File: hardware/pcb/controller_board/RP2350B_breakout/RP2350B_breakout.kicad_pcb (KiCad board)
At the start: 2 copper layers, 54 parts, among them J1 USB_B_Micro, J2 430450828, J4 SM03B-SRSS-TB, J6 debug, SW1 SW_Push, SW2 SW_Push, U1 RP2350_80QFN, U2 NCP1117-3.3_SOT223, U3 W25Q128JVS, U5 ISO7730FDWR, U6 AM26LS31CD, Y1 ABM8-272-T3

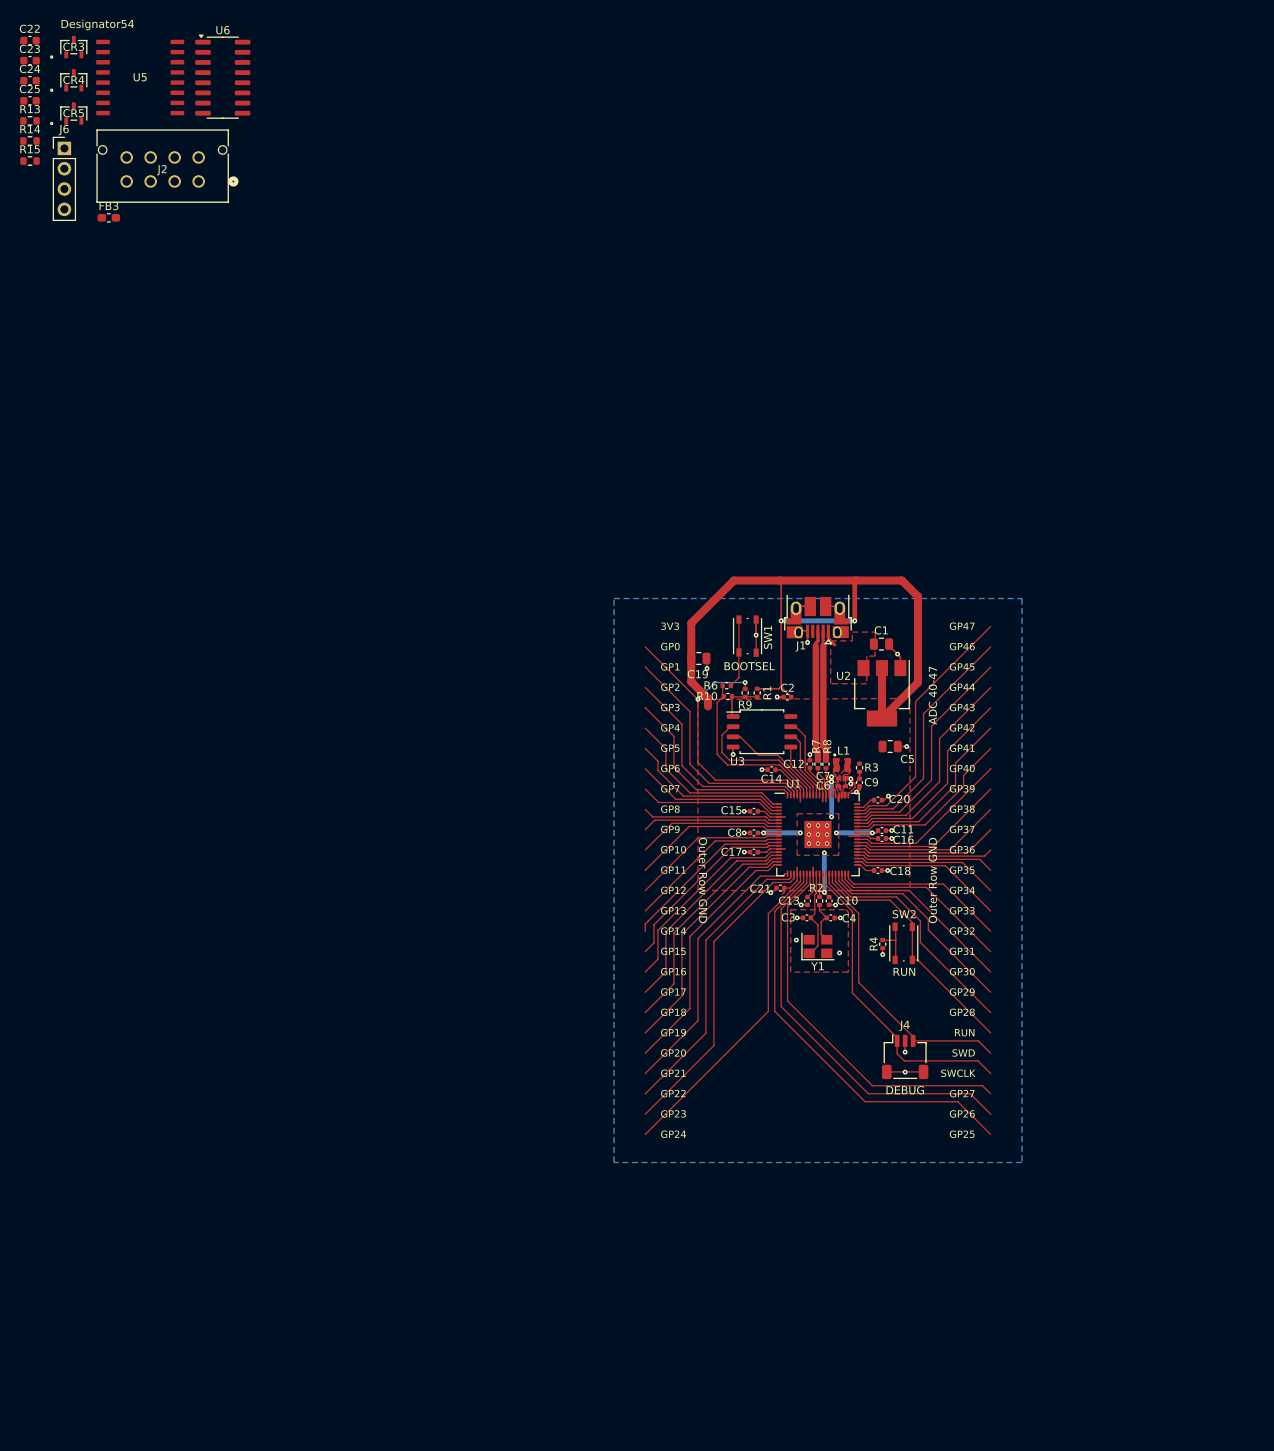
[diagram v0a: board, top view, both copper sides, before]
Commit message: KiCAD files for 6 axis RP2350B board
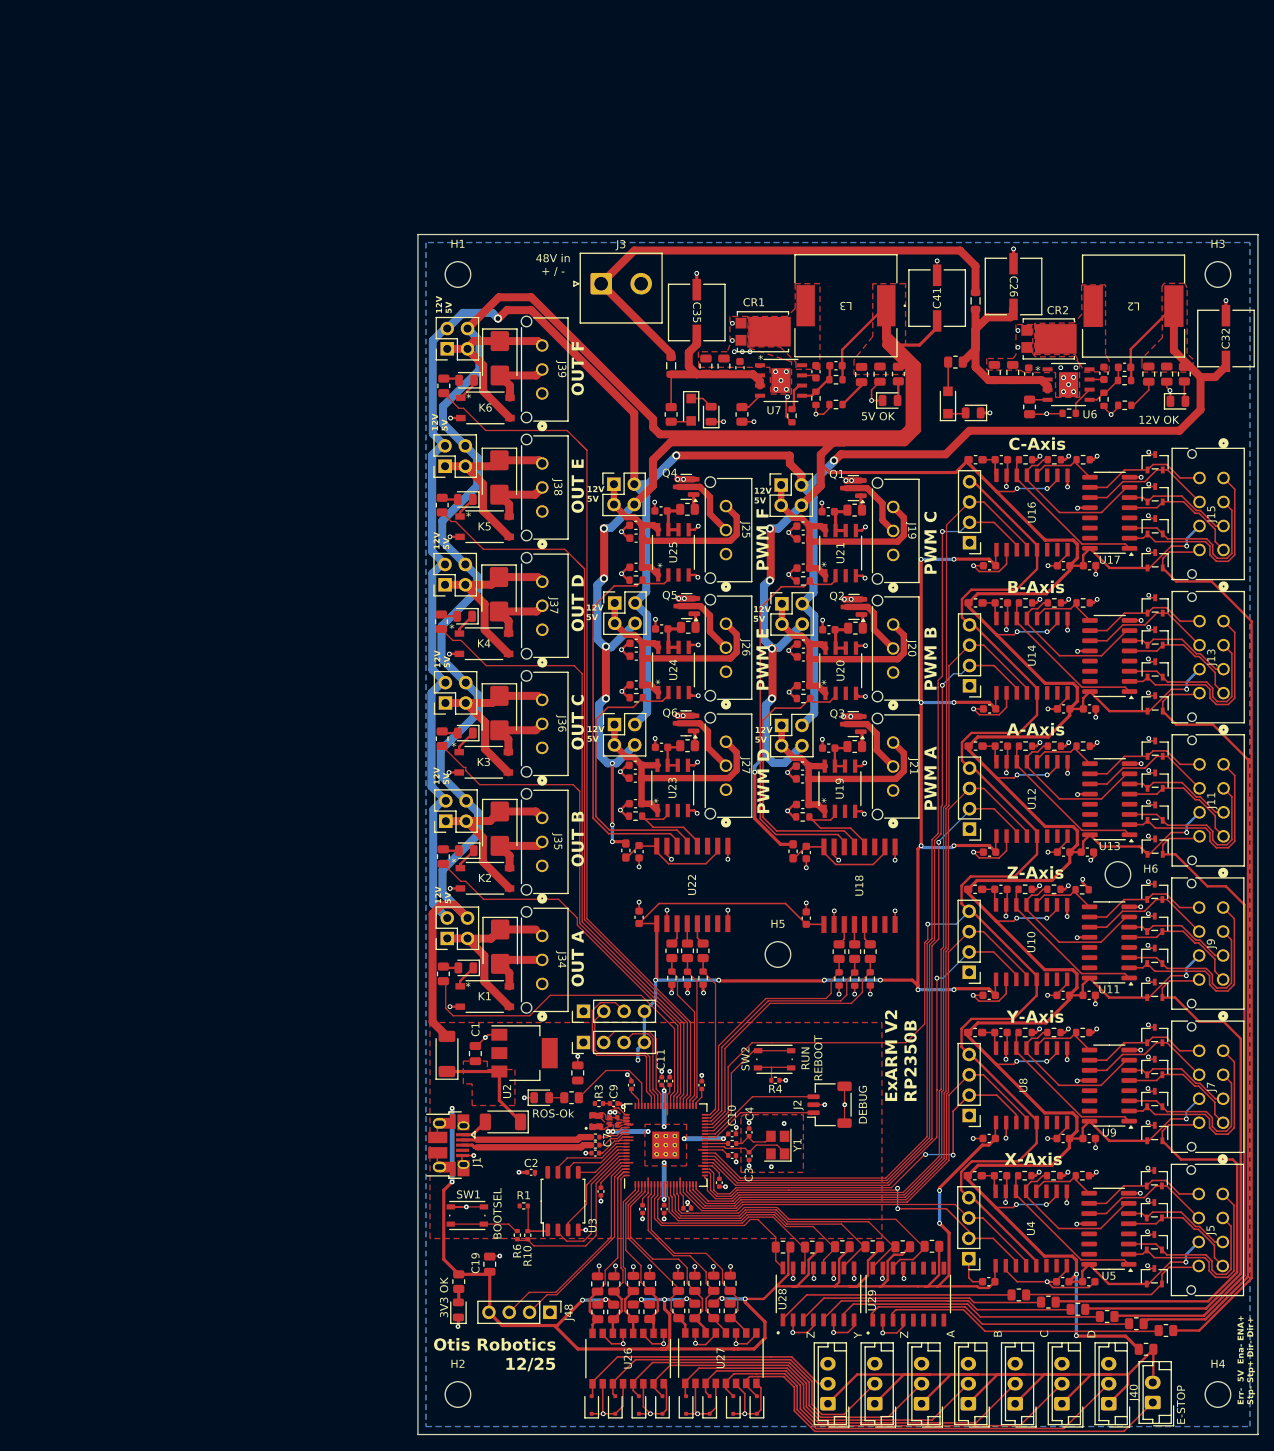
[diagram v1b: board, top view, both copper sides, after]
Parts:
- removed the J2 at (22.6, 18.4)
- added C26: EEE-FK1H470XP, CAP_EEFK_D8_PAN:CAP_EEFK_D8_PAN-L, F.Cu at (124.5, 31.5)
- added C27: 2.2uF, Capacitor_SMD:C_0805_2012Metric, F.Cu at (122.0, 42.2)
- added C28: 2.2uF, Capacitor_SMD:C_0805_2012Metric, F.Cu at (124.3, 42.2)
- added C29: 0.1uF, Capacitor_SMD:C_0603_1608Metric, F.Cu at (126.3, 42.5)
- added C30: 2.2nF, Capacitor_SMD:C_0603_1608Metric, F.Cu at (135.8, 42.4)
- added C31: 50pF, Capacitor_SMD:C_0603_1608Metric, F.Cu at (138.3, 41.6)
- added C32: EEE-FK1H470XP, CAP_EEFK_D8_PAN:CAP_EEFK_D8_PAN-L, F.Cu at (151.0, 38.0)
- added C33: 22uF, Capacitor_SMD:C_0805_2012Metric, F.Cu at (141.3, 42.5)
- added C34: 22uF, Capacitor_SMD:C_0805_2012Metric, F.Cu at (143.6, 42.5)
- added C35: EEE-FK1H470XP, CAP_EEFK_D8_PAN:CAP_EEFK_D8_PAN-L, F.Cu at (84.8, 34.8)
- added C36: 2.2uF, Capacitor_SMD:C_0805_2012Metric, F.Cu at (88.2, 41.5)
- added C37: 2.2uF, Capacitor_SMD:C_0805_2012Metric, F.Cu at (86.0, 41.5)
- added C38: 0.1uF, Capacitor_SMD:C_0603_1608Metric, F.Cu at (90.2, 41.6)
- added C39: 2.2nF, Capacitor_SMD:C_0603_1608Metric, F.Cu at (99.8, 42.1)
- added C40: 65pF, Capacitor_SMD:C_0603_1608Metric, F.Cu at (102.2, 41.4)
- added C41: EEE-FK1H470XP, CAP_EEFK_D8_PAN:CAP_EEFK_D8_PAN-L, F.Cu at (114.9, 32.9)
- added C42: 22uF, Capacitor_SMD:C_0805_2012Metric, F.Cu at (105.5, 42.5)
- added C43: 22uF, Capacitor_SMD:C_0805_2012Metric, F.Cu at (107.8, 42.5)
- added C44: 100nF, Capacitor_SMD:C_0603_1608Metric, F.Cu at (121.4, 138.0)
- added C45: 100nF, Capacitor_SMD:C_0603_1608Metric, F.Cu at (122.9, 124.8)
- added C46: 1uF, Capacitor_SMD:C_0603_1608Metric, F.Cu at (133.9, 138.0)
- added C47: 100nF, Capacitor_SMD:C_0603_1608Metric, F.Cu at (130.7, 138.0)
- added C48: 100nF, Capacitor_SMD:C_0603_1608Metric, F.Cu at (121.4, 120.1)
- added C49: 100nF, Capacitor_SMD:C_0603_1608Metric, F.Cu at (122.9, 106.8)
- added C50: 1uF, Capacitor_SMD:C_0603_1608Metric, F.Cu at (133.9, 120.1)
- added C51: 100nF, Capacitor_SMD:C_0603_1608Metric, F.Cu at (130.7, 120.1)
- added C52: 100nF, Capacitor_SMD:C_0603_1608Metric, F.Cu at (121.5, 102.2)
- added C53: 100nF, Capacitor_SMD:C_0603_1608Metric, F.Cu at (122.9, 89.0)
- added C54: 1uF, Capacitor_SMD:C_0603_1608Metric, F.Cu at (133.7, 102.2)
- added C55: 100nF, Capacitor_SMD:C_0603_1608Metric, F.Cu at (130.7, 102.2)
- added C56: 100nF, Capacitor_SMD:C_0603_1608Metric, F.Cu at (121.5, 84.3)
- added C57: 100nF, Capacitor_SMD:C_0603_1608Metric, F.Cu at (122.9, 71.0)
- added C58: 1uF, Capacitor_SMD:C_0603_1608Metric, F.Cu at (133.9, 84.3)
- added C59: 100nF, Capacitor_SMD:C_0603_1608Metric, F.Cu at (130.7, 84.3)
- added C60: 100nF, Capacitor_SMD:C_0603_1608Metric, F.Cu at (121.5, 66.4)
- added C61: 100nF, Capacitor_SMD:C_0603_1608Metric, F.Cu at (122.9, 53.1)
- added C62: 1uF, Capacitor_SMD:C_0603_1608Metric, F.Cu at (133.9, 66.4)
- added C63: 100nF, Capacitor_SMD:C_0603_1608Metric, F.Cu at (130.7, 66.4)
- added C64: 100nF, Capacitor_SMD:C_0603_1608Metric, F.Cu at (98.5, 110.5)
- added C65: 100nF, Capacitor_SMD:C_0603_1608Metric, F.Cu at (98.5, 102.3)
- added C66: 100nF, Capacitor_SMD:C_0603_1608Metric, F.Cu at (98.1, 96.3)
- added C67: 100nF, Capacitor_SMD:C_0603_1608Metric, F.Cu at (98.2, 81.4)
- added C68: 100nF, Capacitor_SMD:C_0603_1608Metric, F.Cu at (98.2, 66.7)
- added C69: 100nF, Capacitor_SMD:C_0603_1608Metric, F.Cu at (98.1, 91.5)
- added C70: 100nF, Capacitor_SMD:C_0603_1608Metric, F.Cu at (98.2, 76.2)
- added C71: 25pF, Capacitor_SMD:C_0603_1608Metric, F.Cu at (101.3, 89.2)
- added C72: 100nF, Capacitor_SMD:C_0603_1608Metric, F.Cu at (98.1, 61.5)
- added C73: 25pF, Capacitor_SMD:C_0603_1608Metric, F.Cu at (101.4, 74.4)
- added C74: 25pF, Capacitor_SMD:C_0603_1608Metric, F.Cu at (101.3, 59.7)
- added C75: 1uF, Capacitor_SMD:C_0603_1608Metric, F.Cu at (98.1, 93.1)
- added C76: 1uF, Capacitor_SMD:C_0603_1608Metric, F.Cu at (98.2, 77.8)
- added C77: 1uF, Capacitor_SMD:C_0603_1608Metric, F.Cu at (98.2, 63.1)
- added C78: 100nF, Capacitor_SMD:C_0603_1608Metric, F.Cu at (77.6, 110.4)
- added C79: 100nF, Capacitor_SMD:C_0603_1608Metric, F.Cu at (77.6, 102.2)
- added C80: 100nF, Capacitor_SMD:C_0603_1608Metric, F.Cu at (77.2, 96.2)
- added C81: 100nF, Capacitor_SMD:C_0603_1608Metric, F.Cu at (77.3, 81.3)
- added C82: 100nF, Capacitor_SMD:C_0603_1608Metric, F.Cu at (77.3, 66.6)
- added C83: 100nF, Capacitor_SMD:C_0603_1608Metric, F.Cu at (77.2, 91.4)
- added C84: 100nF, Capacitor_SMD:C_0603_1608Metric, F.Cu at (77.3, 76.1)
- added C85: 25pF, Capacitor_SMD:C_0603_1608Metric, F.Cu at (80.5, 89.1)
- added C86: 100nF, Capacitor_SMD:C_0603_1608Metric, F.Cu at (77.2, 61.4)
- added C87: 25pF, Capacitor_SMD:C_0603_1608Metric, F.Cu at (80.5, 74.3)
- added C88: 25pF, Capacitor_SMD:C_0603_1608Metric, F.Cu at (80.4, 59.6)
- added C89: 1uF, Capacitor_SMD:C_0603_1608Metric, F.Cu at (77.2, 93.0)
- added C90: 1uF, Capacitor_SMD:C_0603_1608Metric, F.Cu at (77.3, 77.7)
- added C91: 1uF, Capacitor_SMD:C_0603_1608Metric, F.Cu at (77.3, 63.0)
- added C92: 100nF, Capacitor_SMD:C_0805_2012Metric, F.Cu at (74.5, 156.2)
- added C93: 100nF, Capacitor_SMD:C_0805_2012Metric, F.Cu at (76.9, 156.1)
- added C94: 100nF, Capacitor_SMD:C_0805_2012Metric, F.Cu at (79.0, 156.1)
- added C95: 100nF, Capacitor_SMD:C_0805_2012Metric, F.Cu at (82.6, 156.1)
- added C96: 100nF, Capacitor_SMD:C_0805_2012Metric, F.Cu at (84.6, 156.1)
- added C97: 100nF, Capacitor_SMD:C_0805_2012Metric, F.Cu at (89.0, 156.1)
- added C98: 100nF, Capacitor_SMD:C_0805_2012Metric, F.Cu at (72.5, 156.2)
- added C99: 100nF, Capacitor_SMD:C_0805_2012Metric, F.Cu at (87.0, 156.1)
- added CR1: SS5P10-M3/86A, SS5P10-M3-86A:DIODE_TO-277A-L, F.Cu at (93.1, 37.1)
- added CR10: PESD2CAN_215, PESD2CAN_215:SOT23_TO-236AB_NEX-L, F.Cu at (142.1, 137.3)
- added CR11: PESD2CAN_215, PESD2CAN_215:SOT23_TO-236AB_NEX-L, F.Cu at (142.1, 115.2)
- added CR12: PESD2CAN_215, PESD2CAN_215:SOT23_TO-236AB_NEX-L, F.Cu at (142.1, 111.2)
- added CR13: PESD2CAN_215, PESD2CAN_215:SOT23_TO-236AB_NEX-L, F.Cu at (142.1, 107.2)
- added CR14: PESD2CAN_215, PESD2CAN_215:SOT23_TO-236AB_NEX-L, F.Cu at (142.1, 119.4)
- added CR15: PESD2CAN_215, PESD2CAN_215:SOT23_TO-236AB_NEX-L, F.Cu at (142.2, 97.3)
- added CR16: PESD2CAN_215, PESD2CAN_215:SOT23_TO-236AB_NEX-L, F.Cu at (142.2, 93.3)
- added CR17: PESD2CAN_215, PESD2CAN_215:SOT23_TO-236AB_NEX-L, F.Cu at (142.2, 89.3)
- added CR18: PESD2CAN_215, PESD2CAN_215:SOT23_TO-236AB_NEX-L, F.Cu at (142.2, 101.5)
- added CR19: PESD2CAN_215, PESD2CAN_215:SOT23_TO-236AB_NEX-L, F.Cu at (142.2, 79.4)
- added CR2: SS5P10-M3/86A, SS5P10-M3-86A:DIODE_TO-277A-L, F.Cu at (128.9, 38.0)
- added CR20: PESD2CAN_215, PESD2CAN_215:SOT23_TO-236AB_NEX-L, F.Cu at (142.2, 75.4)
- added CR21: PESD2CAN_215, PESD2CAN_215:SOT23_TO-236AB_NEX-L, F.Cu at (142.2, 71.4)
- added CR22: PESD2CAN_215, PESD2CAN_215:SOT23_TO-236AB_NEX-L, F.Cu at (142.2, 83.6)
- added CR23: PESD2CAN_215, PESD2CAN_215:SOT23_TO-236AB_NEX-L, F.Cu at (142.2, 61.5)
- added CR24: PESD2CAN_215, PESD2CAN_215:SOT23_TO-236AB_NEX-L, F.Cu at (142.2, 57.5)
- added CR25: PESD2CAN_215, PESD2CAN_215:SOT23_TO-236AB_NEX-L, F.Cu at (142.2, 53.5)
- added CR26: PESD2CAN_215, PESD2CAN_215:SOT23_TO-236AB_NEX-L, F.Cu at (142.2, 65.7)
- added CR6: PESD2CAN_215, PESD2CAN_215:SOT23_TO-236AB_NEX-L, F.Cu at (142.1, 155.2)
- added CR7: PESD2CAN_215, PESD2CAN_215:SOT23_TO-236AB_NEX-L, F.Cu at (142.1, 133.1)
- added CR8: PESD2CAN_215, PESD2CAN_215:SOT23_TO-236AB_NEX-L, F.Cu at (142.1, 129.1)
- added CR9: PESD2CAN_215, PESD2CAN_215:SOT23_TO-236AB_NEX-L, F.Cu at (142.1, 125.1)
- added D1: D_Zener, Diode_SMD:Nexperia_CFP3_SOD-123W, F.Cu at (84.2, 46.9)
- added D10: LED (red), LED_SMD:LED_0805_2012Metric, F.Cu at (56.0, 102.0)
- added D11: LED (red), LED_SMD:LED_0805_2012Metric, F.Cu at (55.9, 87.3)
- added D12: LED (red), LED_SMD:LED_0805_2012Metric, F.Cu at (55.8, 72.7)
- added D13: LED (red), LED_SMD:LED_0805_2012Metric, F.Cu at (55.9, 58.1)
- added D14: LED (red), LED_SMD:LED_0805_2012Metric, F.Cu at (56.1, 43.2)
- added D15: SM6T39AY, Diode_SMD:D_SMB, F.Cu at (60.3, 114.0)
- added D16: SM6T39AY, Diode_SMD:D_SMB, F.Cu at (60.2, 99.3)
- added D17: SM6T39AY, Diode_SMD:D_SMB, F.Cu at (60.2, 84.8)
- added D18: SM6T39AY, Diode_SMD:D_SMB, F.Cu at (60.1, 70.0)
- added D19: SM6T39AY, Diode_SMD:D_SMB, F.Cu at (60.2, 55.4)
- added D2: LED, LED_SMD:LED_0805_2012Metric, F.Cu at (86.7, 47.5)
- added D20: SM6T39AY, Diode_SMD:D_SMB, F.Cu at (60.2, 40.5)
- added D21: BAT54J, Diode_SMD:D_SOD-323F, F.Cu at (71.7, 171.3)
- added D22: BAT54J, Diode_SMD:D_SOD-323F, F.Cu at (74.7, 171.3)
- added D23: BAT54J, Diode_SMD:D_SOD-323F, F.Cu at (77.6, 171.3)
- added D24: BAT54J, Diode_SMD:D_SOD-323F, F.Cu at (80.6, 171.3)
- added D25: BAT54J, Diode_SMD:D_SOD-323F, F.Cu at (83.5, 171.3)
- added D26: BAT54J, Diode_SMD:D_SOD-323F, F.Cu at (86.5, 171.3)
- added D27: BAT54J, Diode_SMD:D_SOD-323F, F.Cu at (89.4, 171.3)
- added D28: BAT54J, Diode_SMD:D_SOD-323F, F.Cu at (92.4, 171.3)
- added D29: LED, LED_SMD:LED_0805_2012Metric, F.Cu at (55.1, 159.4)
- added D3: LED, LED_SMD:LED_0805_2012Metric, F.Cu at (109.0, 45.8)
- added D30: LED, LED_SMD:LED_0805_2012Metric, F.Cu at (65.5, 132.9)
- added D4: D_Zener, Diode_SMD:Nexperia_CFP3_SOD-123W, F.Cu at (116.2, 46.0)
- added D5: LED, LED_SMD:LED_0805_2012Metric, F.Cu at (119.4, 47.3)
- added D6: LED, LED_SMD:LED_0805_2012Metric, F.Cu at (145.0, 45.9)
- added D7: LED (red), LED_SMD:LED_0805_2012Metric, F.Cu at (56.0, 116.7)
- added D8: PMEG4010EP,115, Diode_SMD:D_SOD-128, F.Cu at (60.6, 135.9)
- added D9: PMEG4010EP,115, Diode_SMD:D_SOD-128, F.Cu at (53.6, 127.4)
- added FB1: FerriteBead, Inductor_SMD:L_0805_2012Metric, F.Cu at (81.7, 41.4)
- added FB10: FerriteBead, Inductor_SMD:L_0603_1608Metric_Pad1.05x0.95mm_HandSolder, F.Cu at (76.0, 102.0)
- added FB2: FerriteBead, Inductor_SMD:L_0805_2012Metric, F.Cu at (119.7, 33.3)
- added FB4: FerriteBead, Inductor_SMD:L_0603_1608Metric_Pad1.05x0.95mm_HandSolder, F.Cu at (119.7, 124.8)
- added FB5: FerriteBead, Inductor_SMD:L_0603_1608Metric_Pad1.05x0.95mm_HandSolder, F.Cu at (119.7, 106.8)
- added FB6: FerriteBead, Inductor_SMD:L_0603_1608Metric_Pad1.05x0.95mm_HandSolder, F.Cu at (119.7, 89.0)
- added FB7: FerriteBead, Inductor_SMD:L_0603_1608Metric_Pad1.05x0.95mm_HandSolder, F.Cu at (119.7, 71.0)
- added FB8: FerriteBead, Inductor_SMD:L_0603_1608Metric_Pad1.05x0.95mm_HandSolder, F.Cu at (119.7, 53.1)
- added FB9: FerriteBead, Inductor_SMD:L_0603_1608Metric_Pad1.05x0.95mm_HandSolder, F.Cu at (96.9, 102.1)
- added H1: MountingHole, MountingHole:MountingHole_3.2mm_M3_ISO7380, F.Cu at (55.0, 30.0)
- added H2: MountingHole, MountingHole:MountingHole_3.2mm_M3_ISO7380, F.Cu at (55.0, 170.0)
- added H3: MountingHole, MountingHole:MountingHole_3.2mm_M3_ISO7380, F.Cu at (150.0, 30.0)
- added H4: MountingHole, MountingHole:MountingHole_3.2mm_M3_ISO7380, F.Cu at (150.0, 170.0)
- added H5: MountingHole, MountingHole:MountingHole_3.2mm_M3_ISO7380, F.Cu at (95.0, 115.0)
- added H6: MountingHole, MountingHole:MountingHole_3.2mm_M3_ISO7380, F.Cu at (137.5, 105.0)
- added J10: debug, Connector_PinHeader_2.54mm:PinHeader_1x04_P2.54mm_Vertical, F.Cu at (119.0, 99.3)
- added J11: 430450828, 430450828:CONN_SD-43045-010_08_MOL, F.Cu at (150.7, 91.2)
- added J12: debug, Connector_PinHeader_2.54mm:PinHeader_1x04_P2.54mm_Vertical, F.Cu at (119.0, 81.4)
- added J13: 430450828, 430450828:CONN_SD-43045-010_08_MOL, F.Cu at (150.7, 73.3)
- added J14: debug, Connector_PinHeader_2.54mm:PinHeader_1x04_P2.54mm_Vertical, F.Cu at (119.0, 63.5)
- added J15: 430450828, 430450828:CONN_SD-43045-010_08_MOL, F.Cu at (150.7, 55.4)
- added J16: Conn_02x02_Odd_Even, Connector_PinHeader_2.54mm:PinHeader_2x02_P2.54mm_Vertical, F.Cu at (95.5, 86.4)
- added J17: Conn_02x02_Odd_Even, Connector_PinHeader_2.54mm:PinHeader_2x02_P2.54mm_Vertical, F.Cu at (95.5, 71.2)
- added J18: Conn_02x02_Odd_Even, Connector_PinHeader_2.54mm:PinHeader_2x02_P2.54mm_Vertical, F.Cu at (95.4, 56.3)
- added J19: 436500328, 436500328:CONN_SD-43650-010_03_MOL, F.Cu at (109.7, 62.1)
- added J20: 436500328, 436500328:CONN_SD-43650-010_03_MOL, F.Cu at (109.7, 76.8)
- added J21: 436500328, 436500328:CONN_SD-43650-010_03_MOL, F.Cu at (109.7, 91.5)
- added J22: Conn_02x02_Odd_Even, Connector_PinHeader_2.54mm:PinHeader_2x02_P2.54mm_Vertical, F.Cu at (74.6, 86.3)
- added J23: Conn_02x02_Odd_Even, Connector_PinHeader_2.54mm:PinHeader_2x02_P2.54mm_Vertical, F.Cu at (74.6, 71.1)
- added J24: Conn_02x02_Odd_Even, Connector_PinHeader_2.54mm:PinHeader_2x02_P2.54mm_Vertical, F.Cu at (74.5, 56.2)
- added J25: 436500328, 436500328:CONN_SD-43650-010_03_MOL, F.Cu at (88.8, 62.0)
- added J26: 436500328, 436500328:CONN_SD-43650-010_03_MOL, F.Cu at (88.8, 76.7)
- added J27: 436500328, 436500328:CONN_SD-43650-010_03_MOL, F.Cu at (88.8, 91.4)
- added J28: Conn_02x02_Odd_Even, Connector_PinHeader_2.54mm:PinHeader_2x02_P2.54mm_Vertical, F.Cu at (53.7, 113.0)
- added J29: Conn_02x02_Odd_Even, Connector_PinHeader_2.54mm:PinHeader_2x02_P2.54mm_Vertical, F.Cu at (53.5, 98.3)
- added J3: Conn_01x02, Connector_JST:JST_NV_B02P-NV_1x02_P5.00mm_Vertical, F.Cu at (72.9, 31.1)
- added J30: Conn_02x02_Odd_Even, Connector_PinHeader_2.54mm:PinHeader_2x02_P2.54mm_Vertical, F.Cu at (53.4, 83.6)
- added J31: Conn_02x02_Odd_Even, Connector_PinHeader_2.54mm:PinHeader_2x02_P2.54mm_Vertical, F.Cu at (53.4, 68.8)
- added J32: Conn_02x02_Odd_Even, Connector_PinHeader_2.54mm:PinHeader_2x02_P2.54mm_Vertical, F.Cu at (53.4, 54.0)
- added J33: Conn_02x02_Odd_Even, Connector_PinHeader_2.54mm:PinHeader_2x02_P2.54mm_Vertical, F.Cu at (53.7, 39.3)
- added J34: 436500328, 436500328:CONN_SD-43650-010_03_MOL, F.Cu at (65.8, 115.7)
- added J35: 436500328, 436500328:CONN_SD-43650-010_03_MOL, F.Cu at (65.8, 100.9)
- added J36: 436500328, 436500328:CONN_SD-43650-010_03_MOL, F.Cu at (65.8, 86.2)
- added J37: 436500328, 436500328:CONN_SD-43650-010_03_MOL, F.Cu at (65.9, 71.4)
- added J38: 436500328, 436500328:CONN_SD-43650-010_03_MOL, F.Cu at (65.9, 56.6)
- added J39: 436500328, 436500328:CONN_SD-43650-010_03_MOL, F.Cu at (65.8, 41.9)
- added J4: debug, Connector_PinHeader_2.54mm:PinHeader_1x04_P2.54mm_Vertical, F.Cu at (118.8, 153.0)
- added J40: E_stop, Connector_JST:JST_EH_B2B-EH-A_1x02_P2.50mm_Vertical, F.Cu at (141.8, 171.0)
- added J41: x_home, Connector_JST:JST_EH_B3B-EH-A_1x03_P2.50mm_Vertical, F.Cu at (101.2, 171.2)
- added J42: y_home, Connector_JST:JST_EH_B3B-EH-A_1x03_P2.50mm_Vertical, F.Cu at (107.1, 171.2)
- added J43: z_home, Connector_JST:JST_EH_B3B-EH-A_1x03_P2.50mm_Vertical, F.Cu at (113.0, 171.2)
- added J44: a_home, Connector_JST:JST_EH_B3B-EH-A_1x03_P2.50mm_Vertical, F.Cu at (118.8, 171.2)
- added J45: b_home, Connector_JST:JST_EH_B3B-EH-A_1x03_P2.50mm_Vertical, F.Cu at (124.7, 171.2)
- added J46: c_input, Connector_JST:JST_EH_B3B-EH-A_1x03_P2.50mm_Vertical, F.Cu at (130.5, 171.2)
- added J47: d_input, Connector_JST:JST_EH_B3B-EH-A_1x03_P2.50mm_Vertical, F.Cu at (136.3, 171.2)
- added J48: UART, Connector_PinHeader_2.54mm:PinHeader_1x04_P2.54mm_Vertical, F.Cu at (66.5, 159.7)
- added J49: aux1, Connector_PinHeader_2.54mm:PinHeader_1x04_P2.54mm_Vertical, F.Cu at (70.7, 126.0)
- added J5: 430450828, 430450828:CONN_SD-43045-010_08_MOL, F.Cu at (150.6, 144.9)
- added J50: aux2, Connector_PinHeader_2.54mm:PinHeader_1x04_P2.54mm_Vertical, F.Cu at (70.7, 122.1)
- added J7: 430450828, 430450828:CONN_SD-43045-010_08_MOL, F.Cu at (150.7, 127.0)
- added J8: debug, Connector_PinHeader_2.54mm:PinHeader_1x04_P2.54mm_Vertical, F.Cu at (118.9, 117.2)
- added J9: 430450828, 430450828:CONN_SD-43045-010_08_MOL, F.Cu at (150.7, 109.1)
- added K1: G3VM-61VY3, G3VM-61VY3:V-SOP4_special_OMR, F.Cu at (55.3, 119.0)
- added K2: G3VM-61VY3, G3VM-61VY3:V-SOP4_special_OMR, F.Cu at (55.3, 104.2)
- added K3: G3VM-61VY3, G3VM-61VY3:V-SOP4_special_OMR, F.Cu at (55.2, 89.7)
- added K4: G3VM-61VY3, G3VM-61VY3:V-SOP4_special_OMR, F.Cu at (55.2, 74.9)
- added K5: G3VM-61VY3, G3VM-61VY3:V-SOP4_special_OMR, F.Cu at (55.3, 60.3)
- added K6: G3VM-61VY3, G3VM-61VY3:V-SOP4_special_OMR, F.Cu at (55.4, 45.4)
- added L2: 7447709470, 7447709470:IND_1210-WE-PD_WRE, F.Cu at (139.4, 34.0)
- added L3: 7447709220, 7447709470:IND_1210-WE-PD_WRE-L, F.Cu at (103.5, 33.9)
- added Q1: BSS316N, Package_TO_SOT_SMD:SOT-23, F.Cu at (104.4, 56.7)
- added Q2: BSS316N, Package_TO_SOT_SMD:SOT-23, F.Cu at (104.5, 71.6)
- added Q3: BSS316N, Package_TO_SOT_SMD:SOT-23, F.Cu at (104.4, 86.2)
- added Q4: BSS316N, Package_TO_SOT_SMD:SOT-23, F.Cu at (83.5, 56.6)
- added Q5: BSS316N, Package_TO_SOT_SMD:SOT-23, F.Cu at (83.6, 71.5)
- added Q6: BSS316N, Package_TO_SOT_SMD:SOT-23, F.Cu at (83.5, 86.1)
- added R11: 31.6kOhm, Resistor_SMD:R_0805_2012Metric, F.Cu at (126.5, 46.5)
- added R12: 100k, Resistor_SMD:R_0603_1608Metric, F.Cu at (131.4, 47.4)
- added R16: 453k 1%, Resistor_SMD:R_0603_1608Metric, F.Cu at (138.3, 43.2)
- added R17: 48.1k 1%, Resistor_SMD:R_0603_1608Metric, F.Cu at (135.8, 45.6)
- added R18: 2k, Resistor_SMD:R_0805_2012Metric, F.Cu at (145.8, 42.5)
- added R19: 31.6kOhm, Resistor_SMD:R_0805_2012Metric, F.Cu at (90.5, 47.5)
- added R20: 100k, Resistor_SMD:R_0603_1608Metric, F.Cu at (96.8, 47.6)
- added R21: 316k 1%, Resistor_SMD:R_0603_1608Metric, F.Cu at (102.2, 43.1)
- added R22: 100k 1%, Resistor_SMD:R_0603_1608Metric, F.Cu at (99.8, 45.5)
- added R23: 330, Resistor_SMD:R_0805_2012Metric, F.Cu at (110.0, 42.4)
- added R24: 10k, Resistor_SMD:R_0603_1608Metric, F.Cu at (125.9, 124.8)
- added R25: 10k, Resistor_SMD:R_0603_1608Metric, F.Cu at (129.5, 124.8)
- added R26: 10k, Resistor_SMD:R_0603_1608Metric, F.Cu at (133.1, 124.8)
- added R27: 10k, Resistor_SMD:R_0603_1608Metric, F.Cu at (125.9, 106.8)
- added R28: 10k, Resistor_SMD:R_0603_1608Metric, F.Cu at (129.5, 106.8)
- added R29: 10k, Resistor_SMD:R_0603_1608Metric, F.Cu at (133.0, 106.9)
- added R30: 10k, Resistor_SMD:R_0603_1608Metric, F.Cu at (126.0, 89.0)
- added R31: 10k, Resistor_SMD:R_0603_1608Metric, F.Cu at (129.5, 89.0)
- added R32: 10k, Resistor_SMD:R_0603_1608Metric, F.Cu at (133.2, 89.0)
- added R33: 10k, Resistor_SMD:R_0603_1608Metric, F.Cu at (126.0, 71.0)
- added R34: 10k, Resistor_SMD:R_0603_1608Metric, F.Cu at (129.5, 71.0)
- added R35: 10k, Resistor_SMD:R_0603_1608Metric, F.Cu at (133.2, 71.0)
- added R36: 10k, Resistor_SMD:R_0603_1608Metric, F.Cu at (126.0, 53.1)
- added R37: 10k, Resistor_SMD:R_0603_1608Metric, F.Cu at (129.5, 53.1)
- added R38: 10k, Resistor_SMD:R_0603_1608Metric, F.Cu at (133.2, 53.1)
- added R39: 4.7k, Resistor_SMD:R_0603_1608Metric, F.Cu at (102.6, 118.1)
- added R40: 100, Resistor_SMD:R_0805_2012Metric, F.Cu at (102.6, 114.6)
- added R41: 4.7k, Resistor_SMD:R_0603_1608Metric, F.Cu at (104.6, 118.1)
- added R42: 100, Resistor_SMD:R_0805_2012Metric, F.Cu at (104.6, 114.6)
- added R43: 4.7k, Resistor_SMD:R_0603_1608Metric, F.Cu at (106.5, 118.1)
- added R44: 100, Resistor_SMD:R_0805_2012Metric, F.Cu at (106.5, 114.6)
- added R45: 10k, Resistor_SMD:R_0603_1608Metric, F.Cu at (98.2, 68.3)
- added R46: 10k, Resistor_SMD:R_0603_1608Metric, F.Cu at (98.1, 97.8)
- added R47: 10k, Resistor_SMD:R_0603_1608Metric, F.Cu at (98.2, 83.0)
- added R48: 0/10Ohm, Resistor_SMD:R_0805_2012Metric, F.Cu at (104.6, 89.0)
- added R49: 0/10Ohm, Resistor_SMD:R_0805_2012Metric, F.Cu at (104.7, 74.2)
- added R5: 10k, Resistor_SMD:R_0805_2012Metric, F.Cu at (81.7, 47.5)
- added R50: 0/10Ohm, Resistor_SMD:R_0805_2012Metric, F.Cu at (104.6, 59.5)
- added R51: 4.7k, Resistor_SMD:R_0603_1608Metric, F.Cu at (81.7, 118.0)
- added R52: 100, Resistor_SMD:R_0805_2012Metric, F.Cu at (81.7, 114.5)
- added R53: 4.7k, Resistor_SMD:R_0603_1608Metric, F.Cu at (83.7, 118.0)
- added R54: 100, Resistor_SMD:R_0805_2012Metric, F.Cu at (83.7, 114.5)
- added R55: 4.7k, Resistor_SMD:R_0603_1608Metric, F.Cu at (85.6, 118.0)
- added R56: 100, Resistor_SMD:R_0805_2012Metric, F.Cu at (85.6, 114.5)
- added R57: 10k, Resistor_SMD:R_0603_1608Metric, F.Cu at (77.3, 68.2)
- added R58: 10k, Resistor_SMD:R_0603_1608Metric, F.Cu at (77.2, 97.7)
- added R59: 10k, Resistor_SMD:R_0603_1608Metric, F.Cu at (77.3, 82.9)
- added R60: 0/10Ohm, Resistor_SMD:R_0805_2012Metric, F.Cu at (83.7, 88.9)
- added R61: 0/10Ohm, Resistor_SMD:R_0805_2012Metric, F.Cu at (83.8, 74.1)
- added R62: 0/10Ohm, Resistor_SMD:R_0805_2012Metric, F.Cu at (83.7, 59.4)
- added R63: 470, Resistor_SMD:R_0805_2012Metric, F.Cu at (53.2, 117.4)
- added R64: 470, Resistor_SMD:R_0805_2012Metric, F.Cu at (53.2, 102.8)
- added R65: 470, Resistor_SMD:R_0805_2012Metric, F.Cu at (53.0, 88.0)
- added R66: 470, Resistor_SMD:R_0805_2012Metric, F.Cu at (52.9, 73.4)
- added R67: 470, Resistor_SMD:R_0805_2012Metric, F.Cu at (53.0, 58.8)
- added R68: 470, Resistor_SMD:R_0805_2012Metric, F.Cu at (53.2, 43.9)
- added R69: 470, Resistor_SMD:R_0805_2012Metric, F.Cu at (141.0, 164.3)
- added R70: 4.7kOhm, Resistor_SMD:R_0805_2012Metric, F.Cu at (74.5, 159.7)
- added R71: 4.7kOhm, Resistor_SMD:R_0805_2012Metric, F.Cu at (76.9, 159.7)
- added R72: 4.7kOhm, Resistor_SMD:R_0805_2012Metric, F.Cu at (79.0, 159.7)
- added R73: 4.7kOhm, Resistor_SMD:R_0805_2012Metric, F.Cu at (82.6, 159.5)
- added R74: 4.7kOhm, Resistor_SMD:R_0805_2012Metric, F.Cu at (84.6, 159.6)
- added R75: 4.7kOhm, Resistor_SMD:R_0805_2012Metric, F.Cu at (89.0, 159.5)
- added R76: 4.7kOhm, Resistor_SMD:R_0805_2012Metric, F.Cu at (72.5, 159.7)
- added R77: 4.7kOhm, Resistor_SMD:R_0805_2012Metric, F.Cu at (87.0, 159.5)
- added R78: 4.7kOhm, Resistor_SMD:R_0805_2012Metric, F.Cu at (99.3, 151.6)
- added R79: 4.7kOhm, Resistor_SMD:R_0805_2012Metric, F.Cu at (103.0, 151.5)
- added R80: 4.7kOhm, Resistor_SMD:R_0805_2012Metric, F.Cu at (106.8, 151.5)
- added R81: 4.7kOhm, Resistor_SMD:R_0805_2012Metric, F.Cu at (95.6, 151.6)
- added R82: 4.7kOhm, Resistor_SMD:R_0805_2012Metric, F.Cu at (114.2, 151.5)
- added R83: 470, Resistor_SMD:R_0805_2012Metric, F.Cu at (55.1, 155.9)
- added R84: 470, Resistor_SMD:R_0805_2012Metric, F.Cu at (69.2, 132.9)
- added R85: 4.7kOhm, Resistor_SMD:R_0805_2012Metric, F.Cu at (110.6, 151.5)
- added R86: 470, Resistor_SMD:R_0805_2012Metric, F.Cu at (125.1, 157.6)
- added R87: 470, Resistor_SMD:R_0805_2012Metric, F.Cu at (128.8, 158.4)
- added R88: 470, Resistor_SMD:R_0805_2012Metric, F.Cu at (132.5, 159.3)
- added R89: 470, Resistor_SMD:R_0805_2012Metric, F.Cu at (136.2, 160.2)
- added R90: 470, Resistor_SMD:R_0805_2012Metric, F.Cu at (139.8, 161.2)
- added R91: 470, Resistor_SMD:R_0805_2012Metric, F.Cu at (143.5, 162.0)
- added R_ESR1: 20mOhm, Resistor_SMD:R_0603_1608Metric, F.Cu at (102.2, 46.2)
- added R_ESR2: 20mOhm, Resistor_SMD:R_0603_1608Metric, F.Cu at (138.3, 46.4)
- added U10: ISO7730FDWR, ISO7730FDWR:DW0016B_L, F.Cu at (126.7, 113.4)
- added U11: AM26LS31CD, Package_SO:SOIC-16_3.9x9.9mm_P1.27mm, F.Cu at (136.4, 113.5)
- added U12: ISO7730FDWR, ISO7730FDWR:DW0016B_L, F.Cu at (126.8, 95.5)
- added U13: AM26LS31CD, Package_SO:SOIC-16_3.9x9.9mm_P1.27mm, F.Cu at (136.5, 95.6)
- added U14: ISO7730FDWR, ISO7730FDWR:DW0016B_L, F.Cu at (126.8, 77.6)
- added U15: AM26LS31CD, Package_SO:SOIC-16_3.9x9.9mm_P1.27mm, F.Cu at (136.5, 77.7)
- added U16: ISO7730FDWR, ISO7730FDWR:DW0016B_L, F.Cu at (126.8, 59.7)
- added U17: AM26LS31CD, Package_SO:SOIC-16_3.9x9.9mm_P1.27mm, F.Cu at (136.5, 59.8)
- added U18: ISO7730FDWR, ISO7730FDWR:DW0016B_M, F.Cu at (105.2, 106.4)
- added U19: MIC4420YM-TR, MIC4420YM-TR:SOIC-8_M_MCH-M, F.Cu at (102.7, 94.3)
- added U20: MIC4420YM-TR, MIC4420YM-TR:SOIC-8_M_MCH-M, F.Cu at (102.8, 79.5)
- added U21: MIC4420YM-TR, MIC4420YM-TR:SOIC-8_M_MCH-M, F.Cu at (102.8, 64.8)
- added U22: ISO7730FDWR, ISO7730FDWR:DW0016B_M, F.Cu at (84.3, 106.3)
- added U23: MIC4420YM-TR, MIC4420YM-TR:SOIC-8_M_MCH-M, F.Cu at (81.8, 94.2)
- added U24: MIC4420YM-TR, MIC4420YM-TR:SOIC-8_M_MCH-M, F.Cu at (81.9, 79.4)
- added U25: MIC4420YM-TR, MIC4420YM-TR:SOIC-8_M_MCH-M, F.Cu at (81.9, 64.7)
- added U26: TLP291-4GB-TP_ET, TLP291-4-GB-TP-E-T:SO16_TOS, F.Cu at (76.3, 165.5)
- added U27: TLP291-4GB-TP_ET, TLP291-4-GB-TP-E-T:SO16_TOS, F.Cu at (87.9, 165.5)
- added U28: TLP291-4_TP_E_, TLP291-4_TP_E_:SOIC127P700X229-16N, F.Cu at (100.1, 157.4)
- added U29: TLP291-4_TP_E_, TLP291-4_TP_E_:SOIC127P700X229-16N, F.Cu at (111.3, 157.4)
- added U4: ISO7730FDWR, ISO7730FDWR:DW0016B_L, F.Cu at (126.7, 149.2)
- added U7: LM5013QDDARQ1, LM5013QDDARQ1:POWERPAD8_DDA_TEX-L, F.Cu at (95.4, 43.2)
- added U8: ISO7730FDWR, ISO7730FDWR:DW0016B_L, F.Cu at (126.7, 131.3)
- added U9: AM26LS31CD, Package_SO:SOIC-16_3.9x9.9mm_P1.27mm, F.Cu at (136.4, 131.4)
- R9: value DNF -> 10k; footprint Resistor_SMD:R_0402_1005Metric -> Resistor_SMD:R_0805_2012Metric
- U5: value ISO7730FDWR -> AM26LS31CD; footprint ISO7730FDWR:DW0016B_L -> Package_SO:SOIC-16_3.9x9.9mm_P1.27mm
- U6: value AM26LS31CD -> LM5013QDDARQ1; footprint Package_SO:SOIC-16_3.9x9.9mm_P1.27mm -> LM5013QDDARQ1:POWERPAD8_DDA_TEX-L
- moved CR3 201.4 mm to (142.1, 151.0)
- moved C24 200.1 mm to (133.8, 155.9), turned to 180 degrees
- moved C25 196.1 mm to (130.6, 155.9)
- moved C22 196.0 mm to (121.3, 155.9), turned to 180 degrees
- moved CR4 195.4 mm to (142.1, 147.0)
- moved CR5 189.6 mm to (142.1, 143.0)
- moved U5 188.1 mm to (136.4, 149.3), turned to 180 degrees
- moved C23 184.8 mm to (122.8, 142.7), turned to 180 degrees
- moved R15 182.7 mm to (133.1, 142.7)
- moved R14 181.9 mm to (129.4, 142.7)
- moved R13 181.2 mm to (125.8, 142.7)
- moved J6 165.5 mm to (118.9, 135.1), turned to 180 degrees
- moved FB3 161.4 mm to (119.6, 142.7), turned to 180 degrees
- moved U6 112.5 mm to (131.3, 43.8)
- moved J1 80.6 mm to (53.8, 138.8), turned to -90 degrees
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- renumbered J4 to J2
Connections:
- C1 pad 1: VBUS -> Net-(D8-K)
- C22 pad 2: GND2 -> GND
- C23 pad 2: Net-(U5-EN2) -> Net-(U4-VCC2)
- C24 pad 2: Net-(U5-EN2) -> +5V
- C25 pad 2: Net-(U5-EN2) -> +5V
- CR3 pad 1: /axis/X_dir_P -> /axis_1/X_dir_P
- CR3 pad 2: /axis/X_dir_N -> /axis_1/X_dir_N
- CR4 pad 1: /axis/X_step_P -> /axis_1/X_step_P
- CR4 pad 2: /axis/X_step_N -> /axis_1/X_step_N
- CR5 pad 1: /axis/X_ena_P -> /axis_1/X_ena_P
- CR5 pad 2: /axis/X_ena_N -> /axis_1/X_ena_N
- FB3 pad 1: Net-(U5-EN2) -> Net-(U4-VCC2)
- J1 pad 1: VBUS -> Net-(D8-A)
- J6 pad 1: GND2 -> GND
- J6 pad 2: /GPIO3 -> /GPIO23
- J6 pad 3: /GPIO2 -> /GPIO17
- J6 pad 4: /GPIO4 -> /GPIO28
- R13 pad 1: GND -> Net-(U4-OUTA)
- R13 pad 2: Net-(U5-OUTA) -> GND
- R14 pad 1: Net-(U5-OUTC) -> Net-(U4-OUTB)
- R15 pad 1: Net-(U5-OUTB) -> Net-(U4-OUTC)
- R9 pad 1: /GPIO0 -> Net-(U6-EN/UVLO)
- R9 pad 2: /FLASH_SS -> Net-(D4-A)
- U2 pad 3: VBUS -> Net-(D8-K)
- U5 pad 1: +3V3 -> Net-(U4-OUTA)
- U5 pad 10: Net-(U5-EN2) -> /axis_1/X_ena_P
- U5 pad 11: unconnected-(U5-NC-Pad11) -> /axis_1/X_ena_N
- U5 pad 12: Net-(U5-OUTC) -> GND
- U5 pad 13: Net-(U5-OUTB) -> unconnected-(U5-4Z-Pad13)
- U5 pad 14: Net-(U5-OUTA) -> unconnected-(U5-4Y-Pad14)
- U5 pad 15: GND -> unconnected-(U5-4A-Pad15)
- U5 pad 16: Net-(U5-EN2) -> +5V
- U5 pad 2: GND2 -> /axis_1/X_dir_P
- U5 pad 3: /GPIO3 -> /axis_1/X_dir_N
- U5 pad 4: /GPIO2 -> unconnected-(U5-G-Pad4)
- U5 pad 5: /GPIO4 -> /axis_1/X_step_N
- U5 pad 6: unconnected-(U5-NC-Pad6) -> /axis_1/X_step_P
- U5 pad 7: unconnected-(U5-NC-Pad7) -> Net-(U4-OUTB)
- U5 pad 8: GND2 -> GND
- U5 pad 9: GND -> Net-(U4-OUTC)
- U6 pad 1: Net-(U5-OUTA) -> GND
- U6 pad 2: /axis/X_dir_P -> Net-(U6-EN/UVLO)
- U6 pad 3: /axis/X_dir_N -> Net-(U6-EN/UVLO)
- U6 pad 4: unconnected-(U6-G-Pad4) -> Net-(U6-RON)
- U6 pad 5: /axis/X_step_N -> Net-(U6-FB)
- U6 pad 6: /axis/X_step_P -> Net-(U6-PGOOD)
- U6 pad 7: Net-(U5-OUTB) -> Net-(U6-BST)
- U6 pad 8: GND -> Net-(U6-SW)
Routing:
- net +5V: track 0.00 -> 828.6 mm, vias 0 -> 32
- net GND: track 38.8 -> 443.9 mm, vias 29 -> 237
- net +12V: track 0.00 -> 295.4 mm, vias 0 -> 3
- net +3V3: track 137.4 -> 424.0 mm, vias 2 -> 24
- net /GPIO28: track 28.7 -> 212.6 mm, vias 0 -> 1
- net /C_err: track 0.00 -> 114.7 mm
- net /B_err: track 0.00 -> 99.5 mm
- net /Homing_Estop/V_switch: track 0.00 -> 93.6 mm
- net /GPIO21: track 34.2 -> 126.9 mm
- net /GPIO35: track 17.5 -> 109.9 mm
- net /A_err: track 0.00 -> 83.7 mm
- net /GPIO20: track 31.7 -> 109.6 mm
- net /GPIO36: track 17.2 -> 94.5 mm
- net /GPIO27: track 47.3 -> 119.2 mm, vias 0 -> 1
- net /Z_err: track 0.00 -> 68.8 mm
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- added copper zone on F.Cu, net +12V
- added copper zone on F.Cu, net +5V
- added copper zone on F.Cu, net Net-(D8-K)
- added copper zone on F.Cu, net Net-(U6-SW)
- added copper zone on F.Cu, net Net-(U7-SW)
- removed copper zone on F.Cu, net VBUS
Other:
- board outline added: 105 x 150 mm
- board text added: "12V 5V"
- board text added: "12V OK"
- board text added: "3V3 OK"
- board text added: "48V in + / -"
- board text added: "5V OK"
- board text added: "A"
- board text added: "A-Axis"
- board text added: "B"
- board text added: "B-Axis"
- board text added: "C"
- board text added: "C-Axis"
- board text added: "D"
- board text added: "E-STOP"
- board text added: "Err- 5V Ena- ENA+ Stp- Stp+ Dir- Dir+"
- board text added: "ExARM V2 RP2350B"
- board text added: "OUT A"
- board text added: "OUT B"
- board text added: "OUT C"
- board text added: "OUT D"
- board text added: "OUT E"
- board text added: "OUT F"
- board text added: "Otis Robotics 12/25"
- board text added: "PWM A"
- board text added: "PWM B"
- board text added: "PWM C"
- board text added: "PWM D"
- board text added: "PWM E"
- board text added: "PWM F"
- board text added: "ROS-Ok"
- board text added: "RUN REBOOT"
- board text added: "X-Axis"
- board text added: "Y"
- board text added: "Y-Axis"
- board text added: "Z"
- board text added: "Z-Axis"
- board text removed: "3V3"
- board text removed: "ADC 40-47"
- board text removed: "GP0"
- board text removed: "GP1"
- board text removed: "GP10"
- board text removed: "GP11"
- board text removed: "GP12"
- board text removed: "GP13"
- board text removed: "GP14"
- board text removed: "GP15"
- board text removed: "GP16"
- board text removed: "GP17"
- board text removed: "GP18"
- board text removed: "GP19"
- board text removed: "GP2"
- board text removed: "GP20"
- board text removed: "GP21"
- board text removed: "GP22"
- board text removed: "GP23"
- board text removed: "GP24"
- board text removed: "GP25"
- board text removed: "GP26"
- board text removed: "GP27"
- board text removed: "GP28"
- board text removed: "GP29"
- board text removed: "GP3"
- board text removed: "GP30"
- board text removed: "GP31"
- board text removed: "GP32"
- board text removed: "GP33"
- board text removed: "GP34"
- board text removed: "GP35"
- board text removed: "GP36"
- board text removed: "GP37"
- board text removed: "GP38"
- board text removed: "GP39"
- board text removed: "GP4"
- board text removed: "GP40"
- board text removed: "GP41"
- board text removed: "GP42"
- board text removed: "GP43"
- board text removed: "GP44"
- board text removed: "GP45"
- board text removed: "GP46"
- board text removed: "GP47"
- board text removed: "GP5"
- board text removed: "GP6"
- board text removed: "GP7"
- board text removed: "GP8"
- board text removed: "GP9"
- board text removed: "Outer Row GND"
- board text removed: "RUN"
- board text removed: "SWCLK"
- board text removed: "SWD"
